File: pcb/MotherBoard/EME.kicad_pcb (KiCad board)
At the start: 2 copper layers, 100 x 60 mm, 58 parts, among them J1 BMP180, J10 Reset, J11 UART2, J12 SPI_CONN, J13 UART0, J14 GPIO's, J17 Anemómetro, J19 I2C, J2 volti, J20 Jumper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

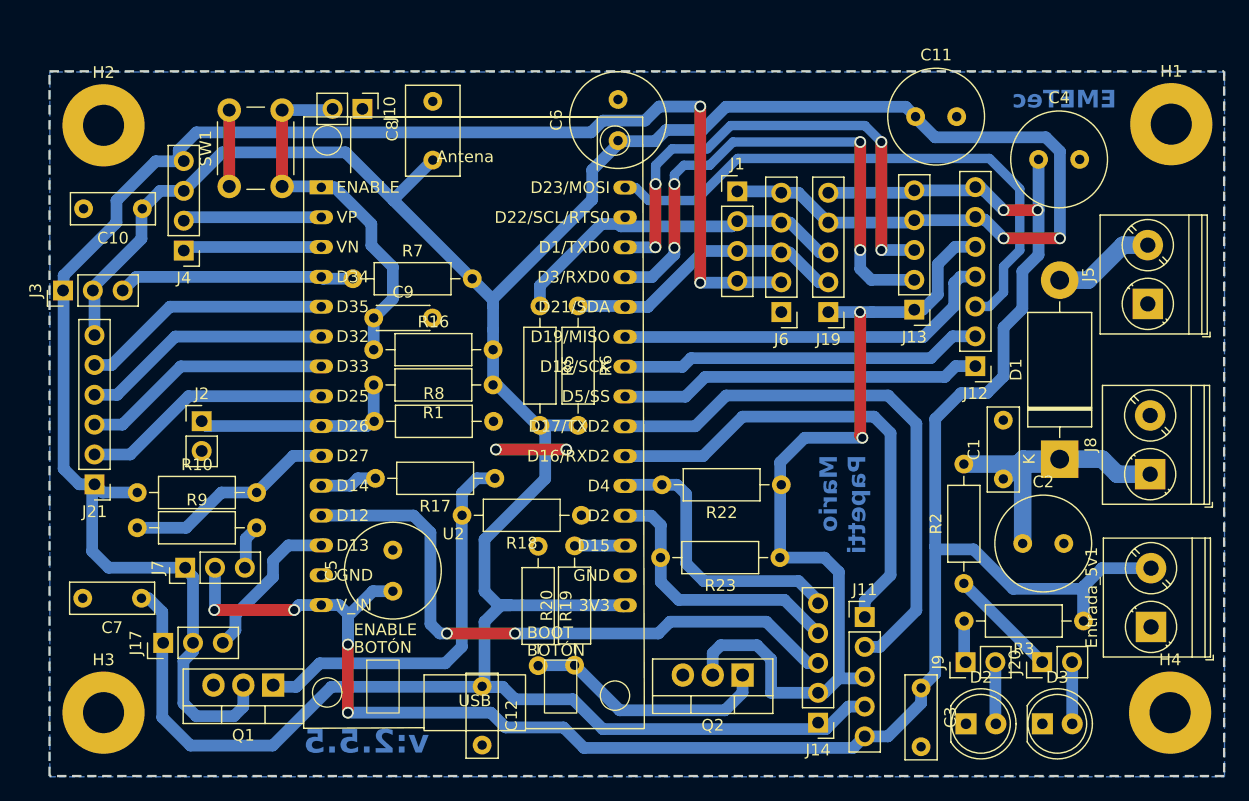
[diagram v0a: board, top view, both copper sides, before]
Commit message: "se modificó conexión del DHT22 a otro pin, se agregó jumper G-g1 y g2, también conectores para extraer alimentación"
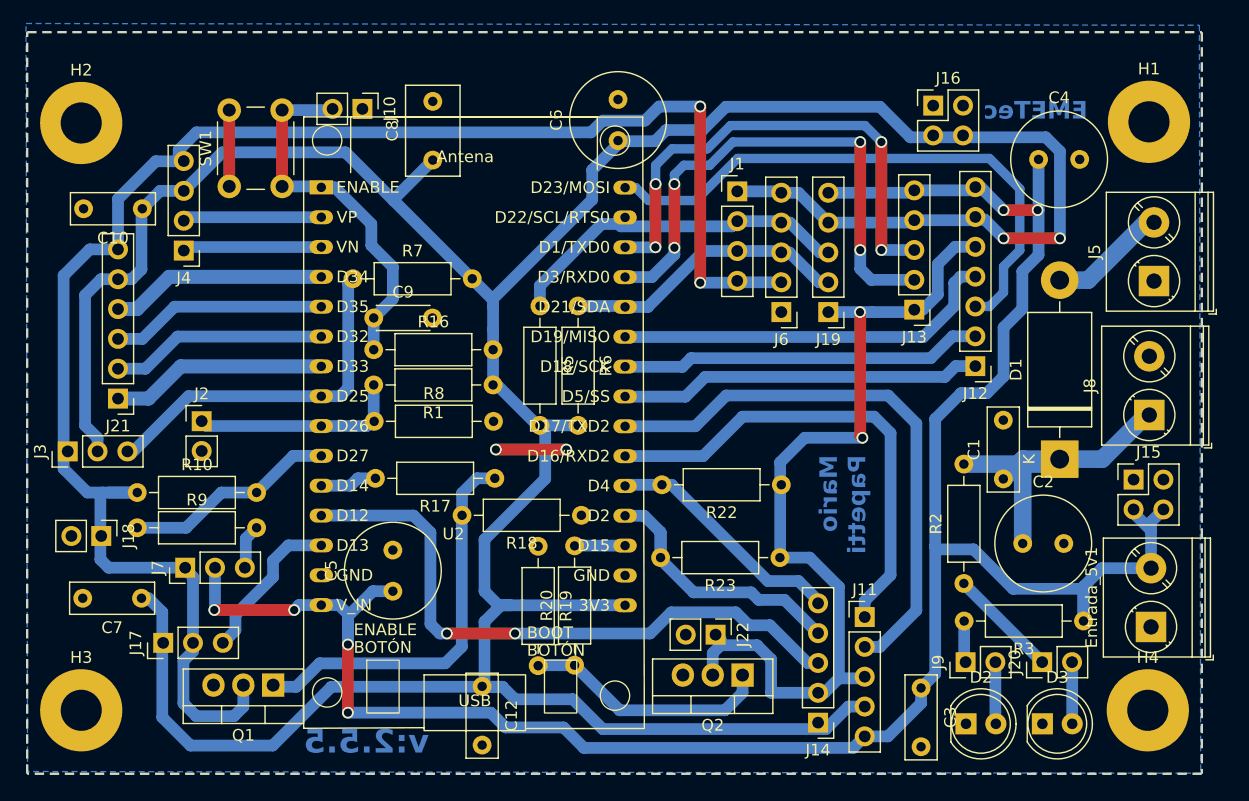
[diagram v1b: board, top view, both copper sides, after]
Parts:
- removed C11: 22uF, Capacitor_THT:C_Radial_D8.0mm_H7.0mm_P3.50mm
- added J15: Alimentaciones, Connector_PinHeader_2.54mm:PinHeader_2x02_P2.54mm_Vertical, F.Cu at (161.7, 97.3)
- added J16: Alimentaciones, Connector_PinHeader_2.54mm:PinHeader_2x02_P2.54mm_Vertical, F.Cu at (144.6, 65.5)
- added J18: G->G1, Connector_PinHeader_2.54mm:PinHeader_1x02_P2.54mm_Vertical, F.Cu at (73.8, 102.1)
- added J22: G->G2, Connector_PinHeader_2.54mm:PinHeader_1x02_P2.54mm_Vertical, F.Cu at (126.1, 110.5)
- moved J3 13.7 mm to (70.9, 94.9)
- moved J21 7.57 mm to (75.2, 90.4)
- moved J8 5.04 mm to (163.0, 91.8)
- moved J5 2.01 mm to (163.4, 80.4)
- moved H1 1.91 mm to (163.0, 66.8)
- moved H2 1.91 mm to (72.1, 66.9)
- moved H3 1.91 mm to (72.1, 116.9)
- moved H4 1.91 mm to (162.9, 116.9)
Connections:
- J21 pad 1: GND_G1 -> Y
- J21 pad 2: Y -> S2
- J21 pad 3: S2 -> S1
- J21 pad 4: S1 -> S0
- J21 pad 5: S0 -> +3.3V
- J21 pad 6: +3.3V -> GND_G1
- U2 pad 4: DHT22 -> S0
- U2 pad 5: S0 -> S1
- U2 pad 6: S1 -> S2
- U2 pad 7: S2 -> Y
- U2 pad 8: Y -> DHT22
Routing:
- net +3.3V: track 280.8 -> 292.8 mm
- net DHT22: track 20.1 -> 30.4 mm
- net +5V: track 180.0 -> 187.8 mm
- net GPIO4: track 24.2 -> 20.8 mm
- net GND_G1: track 141.2 -> 144.4 mm
- net S0: track 21.4 -> 18.4 mm
- net S2: track 21.4 -> 18.4 mm
- net S1: track 21.4 -> 18.4 mm
- net Y: track 21.4 -> 18.4 mm
- net Net-(D1-A): track 8.73 -> 10.1 mm
- net +BATT: track 29.3 -> 30.2 mm
- net GPIO2: track 23.4 -> 24.1 mm
- net GPIO12: track 52.9 -> 53.6 mm
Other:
- board size 100 x 60 mm -> 100 x 63.1 mm
